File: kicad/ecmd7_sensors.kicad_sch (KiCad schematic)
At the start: 43 parts, among them U10 FIN1002M5X, U11 FIN1002M5X, U12 FIN1002M5X, U13 ADM3490ExR, U17 TMP122AIDBVR

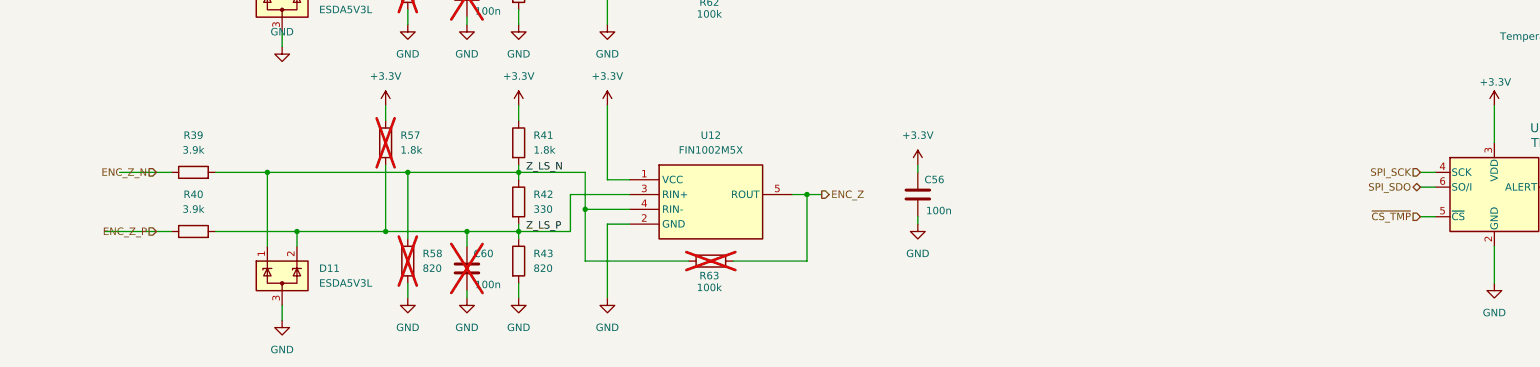
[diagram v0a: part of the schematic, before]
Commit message: Cleanup schematic, add busses
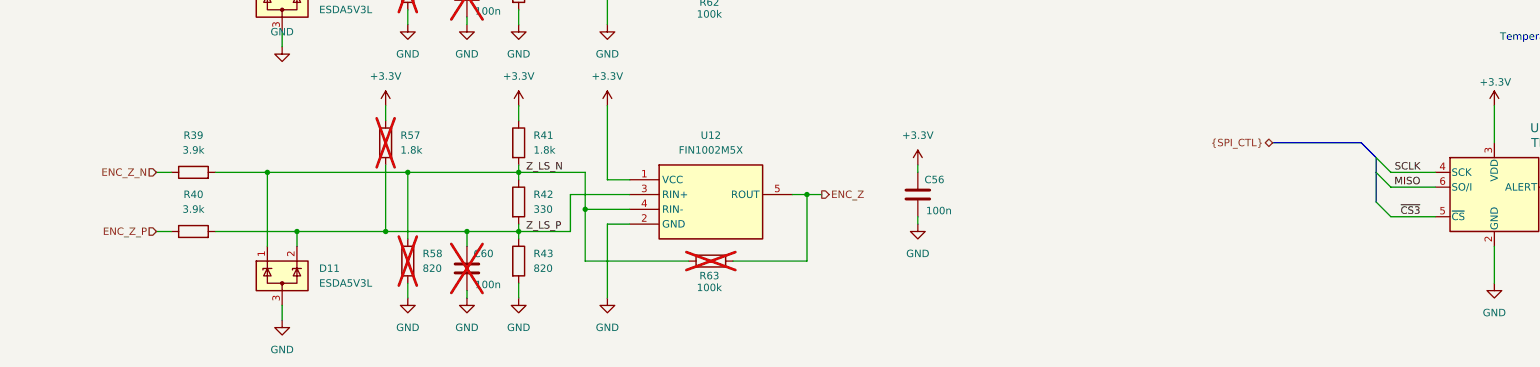
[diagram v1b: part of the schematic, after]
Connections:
- net SPI_SCK renamed SCLK
- net SPI_SDO renamed MISO
- net ~{CS_TMP} renamed ~{CS3}
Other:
- title: (none) -> ECMD7 Sensor Inputs
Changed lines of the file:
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@@
 	(generator_version "9.0")
 	(paper "A3")
+	(title_block
+		(title "ECMD7 Sensor Inputs")
+		(date "2025-11-12")
+		(rev "1.0")
+	)
 	(text "Temperature Sensor"
 		(exclude_from_sim no)
@@
 		(at 322.58 177.8)
 	)
+	(bus_entry
+		(at 292.1 175.26)
+		(size 2.54 2.54)
+		(stroke
+			(width 0)
+			(type default)
+		)
+	)
+	(bus_entry
+		(at 292.1 172.72)
+		(size 2.54 2.54)
+		(stroke
+			(width 0)
+			(type default)
+		)
+	)
+	(bus_entry
+		(at 292.1 180.34)
+		(size 2.54 2.54)
+		(stroke
+			(width 0)
+			(type default)
+		)
+	)
 	(wire
 		(pts
@@
 		)
 	)
+	(bus
+		(pts
+			(xy 292.1 172.72) (xy 289.56 170.18)
+		)
+		(stroke
+			(width 0)
+			(type default)
+		)
+	)
+	(wire
+		(pts
+			(xy 294.64 175.26) (xy 302.26 175.26)
+		)
+		(stroke
+			(width 0)
+			(type default)
+		)
+	)
 	(wire
 		(pts
@@
 	(wire
 		(pts
+			(xy 294.64 177.8) (xy 302.26 177.8)
+		)
+		(stroke
+			(width 0)
+			(type default)
+		)
+	)
+	(wire
+		(pts
 			(xy 194.31 143.51) (xy 194.31 132.08)
 		)
@@
 		)
 	)
+	(bus
+		(pts
+			(xy 292.1 175.26) (xy 292.1 180.34)
+		)
+		(stroke
+			(width 0)
+			(type default)
+		)
+	)
 	(wire
 		(pts
@@
 	(wire
 		(pts
-			(xy 73.66 185.42) (xy 85.09 185.42)
-		)
-		(stroke
-			(width 0)
-			(type default)
-		)
-	)
-	(wire
-		(pts
 			(xy 144.78 99.06) (xy 144.78 101.6)
 		)
@@
 	(wire
 		(pts
-			(xy 299.72 177.8) (xy 302.26 177.8)
-		)
-		(stroke
-			(width 0)
-			(type default)
-		)
-	)
-	(wire
-		(pts
 			(xy 194.31 179.07) (xy 194.31 190.5)
 		)
@@
 	(wire
 		(pts
+			(xy 82.55 185.42) (xy 85.09 185.42)
+		)
+		(stroke
+			(width 0)
+			(type default)
+		)
+	)
+	(wire
+		(pts
+			(xy 82.55 175.26) (xy 85.09 175.26)
+		)
+		(stroke
+			(width 0)
+			(type default)
+		)
+	)
+	(wire
+		(pts
 			(xy 181.61 95.25) (xy 194.31 95.25)
 		)
@@
 	(wire
 		(pts
-			(xy 76.2 175.26) (xy 85.09 175.26)
-		)
-		(stroke
-			(width 0)
-			(type default)
-		)
-	)
-	(wire
-		(pts
 			(xy 163.83 137.16) (xy 160.02 137.16)
 		)
@@
 	(wire
 		(pts
+			(xy 294.64 182.88) (xy 302.26 182.88)
+		)
+		(stroke
+			(width 0)
+			(type default)
+		)
+	)
+	(wire
+		(pts
 			(xy 135.89 138.43) (xy 135.89 140.97)
 		)
@@
 		)
 	)
+	(bus
+		(pts
+			(xy 274.32 170.18) (xy 289.56 170.18)
+		)
+		(stroke
+			(width 0)
+			(type default)
+		)
+	)
 	(wire
 		(pts
@@
 	(wire
 		(pts
-			(xy 299.72 182.88) (xy 302.26 182.88)
-		)
-		(stroke
-			(width 0)
-			(type default)
-		)
-	)
-	(wire
-		(pts
 			(xy 135.89 100.33) (xy 135.89 101.6)
 		)
@@
 	(wire
 		(pts
-			(xy 299.72 175.26) (xy 302.26 175.26)
-		)
-		(stroke
-			(width 0)
-			(type default)
-		)
-	)
-	(wire
-		(pts
 			(xy 144.78 128.27) (xy 156.21 128.27)
 		)
@@
 		(pts
 			(xy 300.99 107.95) (xy 300.99 110.49)
+		)
+		(stroke
+			(width 0)
+			(type default)
+		)
+	)
+	(bus
+		(pts
+			(xy 292.1 172.72) (xy 292.1 175.26)
 		)
 		(stroke
@@
 		)
 	)
+	(label "MISO"
+		(at 299.72 177.8 180)
+		(effects
+			(font
+				(size 1.27 1.27)
+			)
+			(justify right bottom)
+		)
+	)
 	(label "Z_LS_N"
 		(at 146.05 175.26 0)
@@
 		)
 	)
+	(label "SCLK"
+		(at 299.72 175.26 180)
+		(effects
+			(font
+				(size 1.27 1.27)
+			)
+			(justify right bottom)
+		)
+	)
 	(label "B_LS_P"
 		(at 146.05 138.43 0)
@@
 			)
 			(justify left bottom)
+		)
+	)
+	(label "~{CS3}"
+		(at 299.72 182.88 180)
+		(effects
+			(font
+				(size 1.27 1.27)
+			)
+			(justify right bottom)
 		)
 	)
@@
 		)
 	)
-	(hierarchical_label "SPI_SCK"
-		(shape input)
-		(at 299.72 175.26 180)
-		(effects
-			(font
-				(size 1.27 1.27)
-			)
-			(justify right)
-		)
-	)
-	(hierarchical_label "SPI_SDO"
-		(shape tri_state)
-		(at 299.72 177.8 180)
+	(hierarchical_label "{SPI_CTL}"
+		(shape bidirectional)
+		(at 274.32 170.18 180)
 		(effects
 			(font
@@
 		)
 	)
-	(hierarchical_label "~{CS_TMP}"
-		(shape input)
-		(at 299.72 182.88 180)
-		(effects
-			(font
-				(size 1.27 1.27)
-			)
-			(justify right)
-		)
-	)

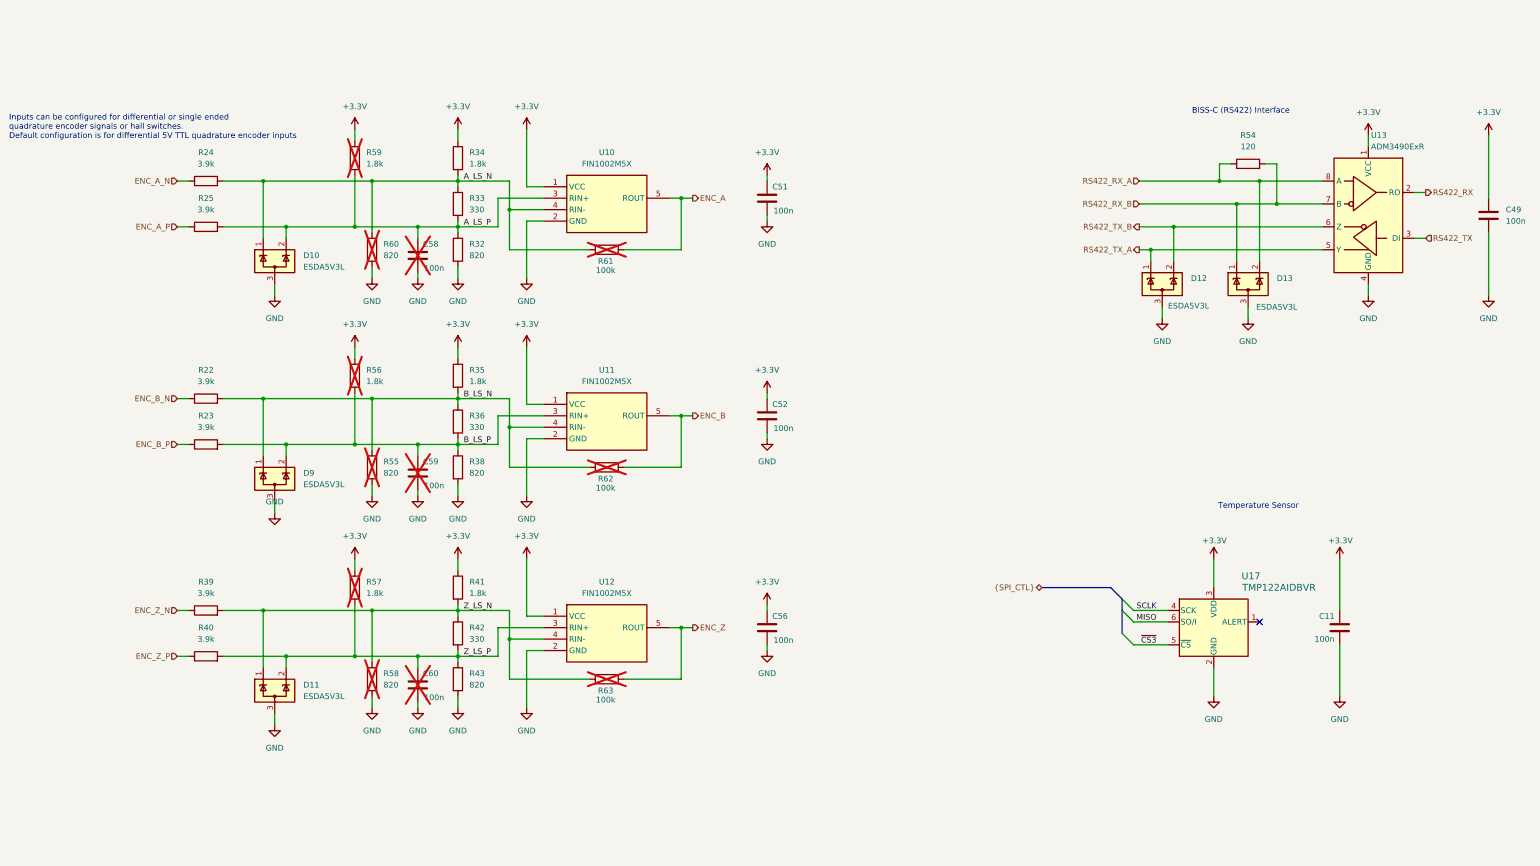
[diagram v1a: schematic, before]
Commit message: General schematic cleanup
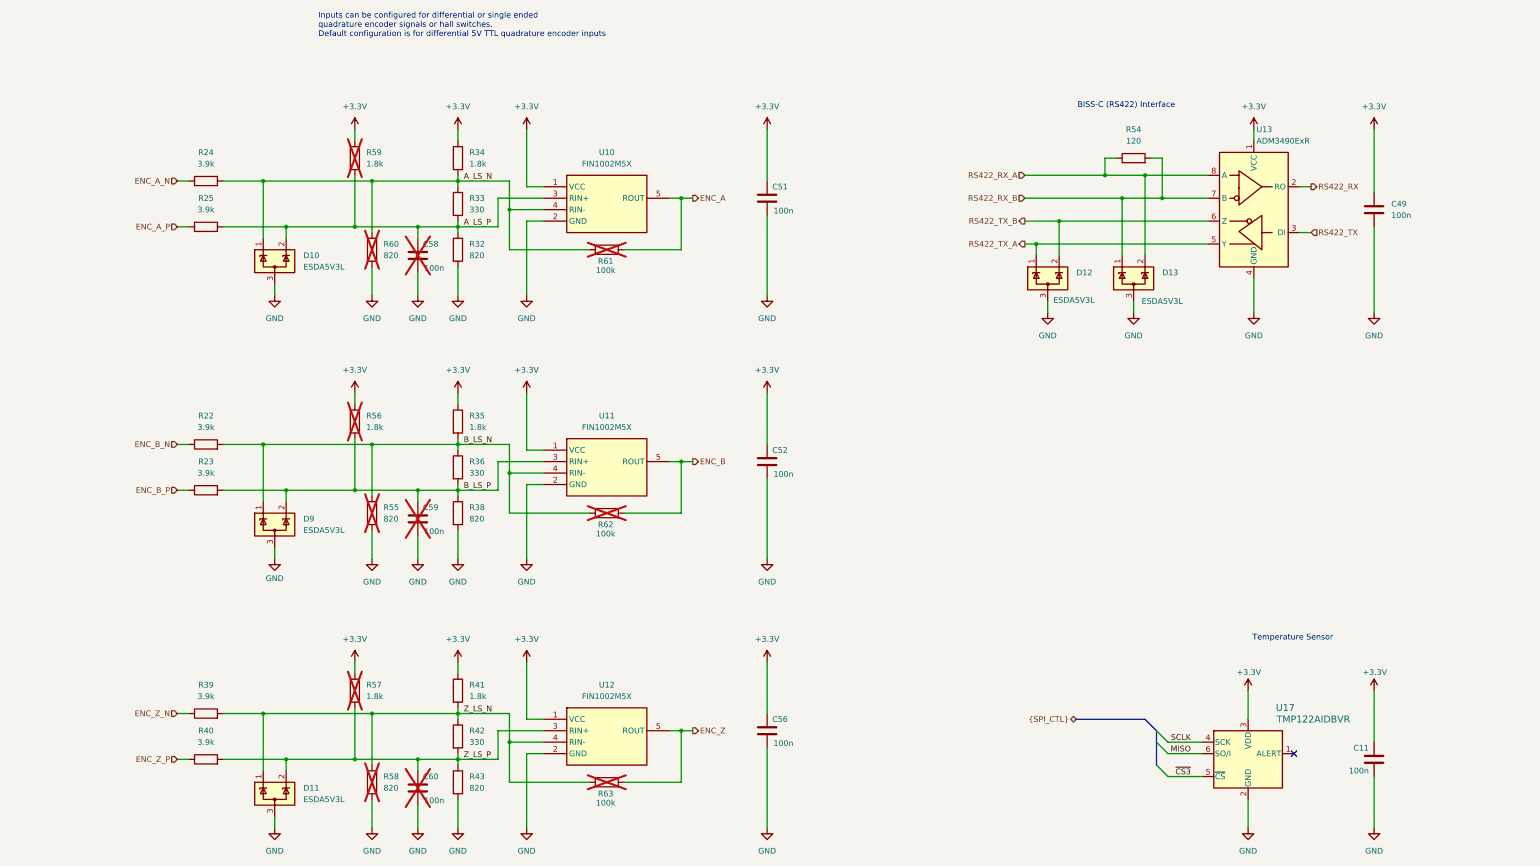
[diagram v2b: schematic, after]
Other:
- moved on the sheet: C11, C49, C52, C56, C59, C60, D11, D12, D13, D9, R22, R23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
